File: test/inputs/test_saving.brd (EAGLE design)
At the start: 160 x 100 mm, 16 parts

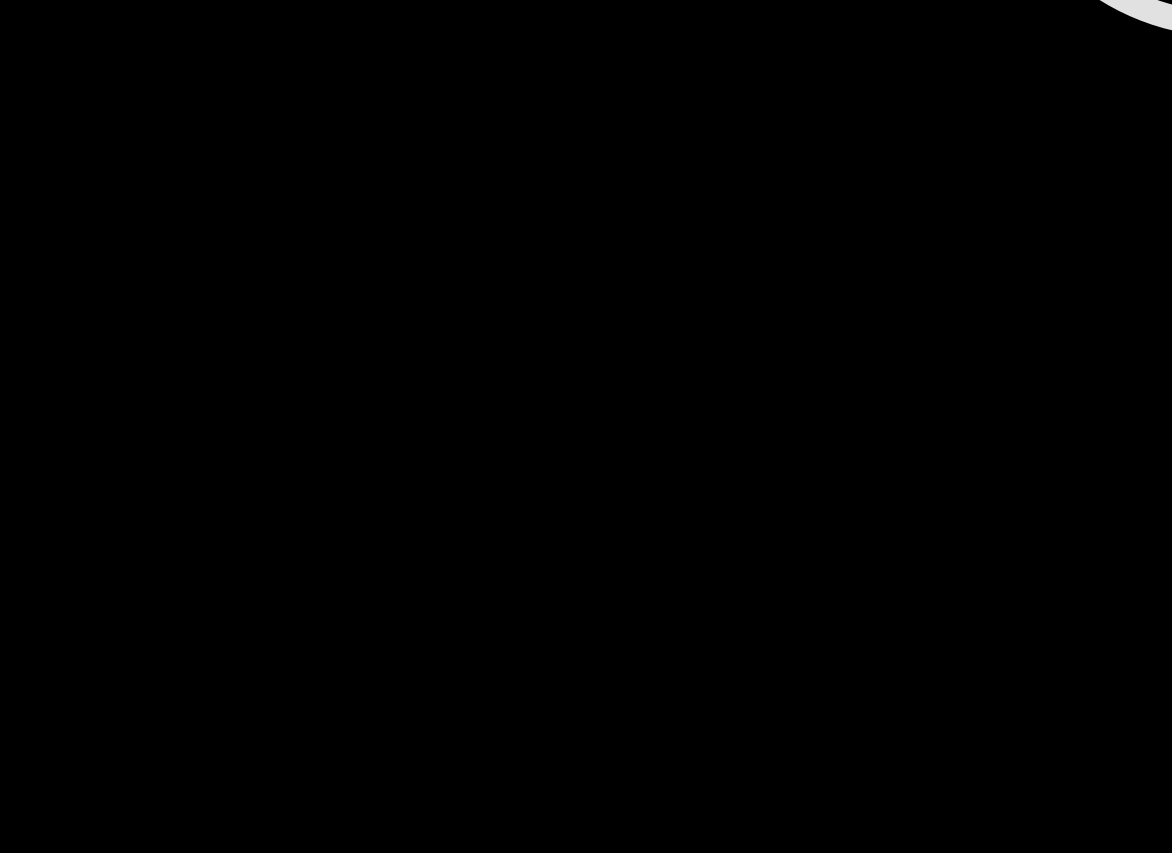
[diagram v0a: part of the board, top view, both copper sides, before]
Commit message: Significantly cleaned up the monkey patch chaos. Rather than use isinstance() or monkey patching, I tried to take advantage of duck typing and hasattr().
Mirroring each individual child element of a package in SwoopGeom should now look exactly the same as if you mirrored the whole package in Eagle. 


git-svn-id: svn+ssh://bbfs-01.calit2.net/grw/Gordon/svn/trunk/Gadgets/Tools/CircuitsByCode@20901 2cf53259-273a-af40-bda6-69d31023b8ec
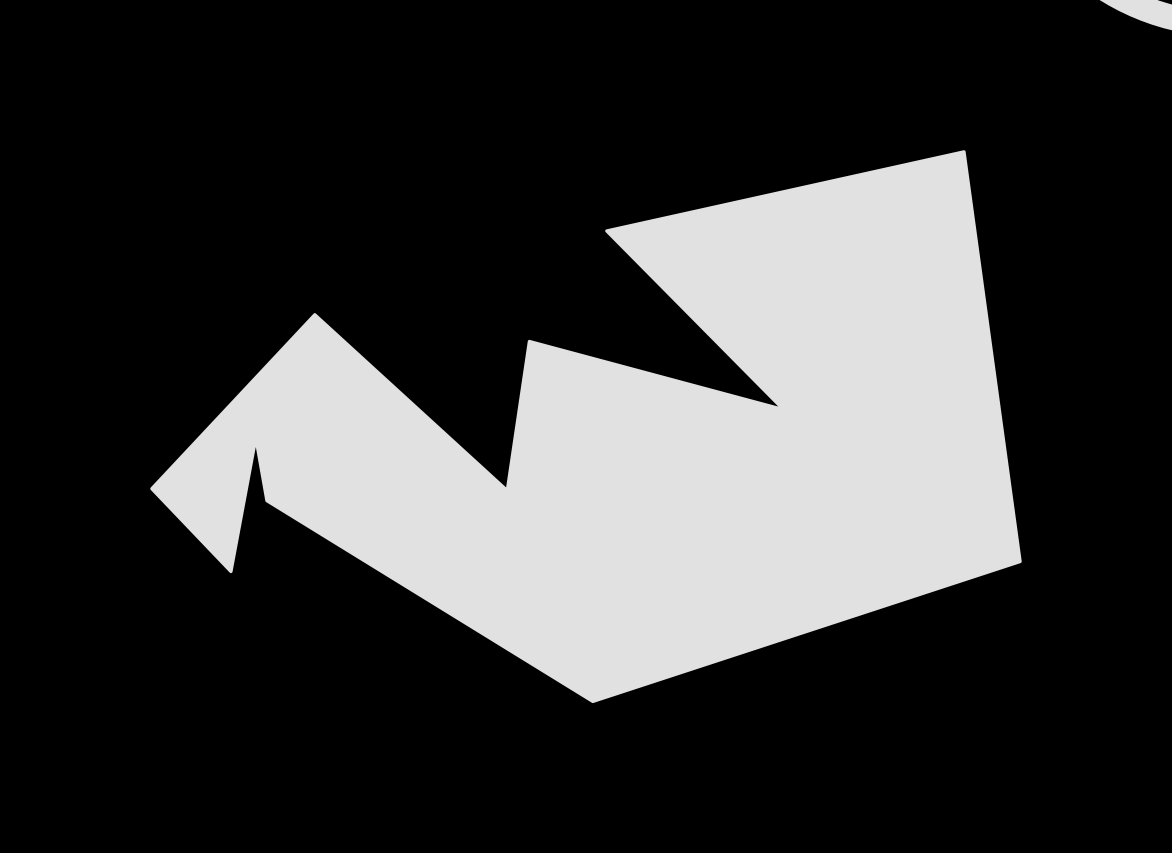
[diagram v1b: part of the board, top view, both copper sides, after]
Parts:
- added TEST-POLYGON: (no value), Swoop-Test-Packages:TEST-POLYGON
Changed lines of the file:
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@@
 <element name="TEST-CIRCLE" library="Swoop-Test-Packages" package="TEST-CIRCLE" value="TEST-CIRCLE" x="150" y="57"/>
 <element name="TEST-HOLE" library="Swoop-Test-Packages" package="TEST-HOLE" value="TEST-HOLE" x="115" y="58"/>
+<element name="TEST-POLYGON" library="Swoop-Test-Packages" package="TEST-POLYGON" value="" x="119" y="34" rot="R10"/>
 </elements>
 <signals>
